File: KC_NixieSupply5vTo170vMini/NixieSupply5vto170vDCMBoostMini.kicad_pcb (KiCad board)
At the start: 2 copper layers, 38.6 x 29 mm, 42 parts, among them J1 Screw_Terminal_01x04, J2 CONN_01X01, J3 CONN_01X01, J4 CONN_01X01, J5 CONN_01X01, P1 USB_OTG, Q1 FDS2672CT, Q26 MMBTA42, U1 UCC3803

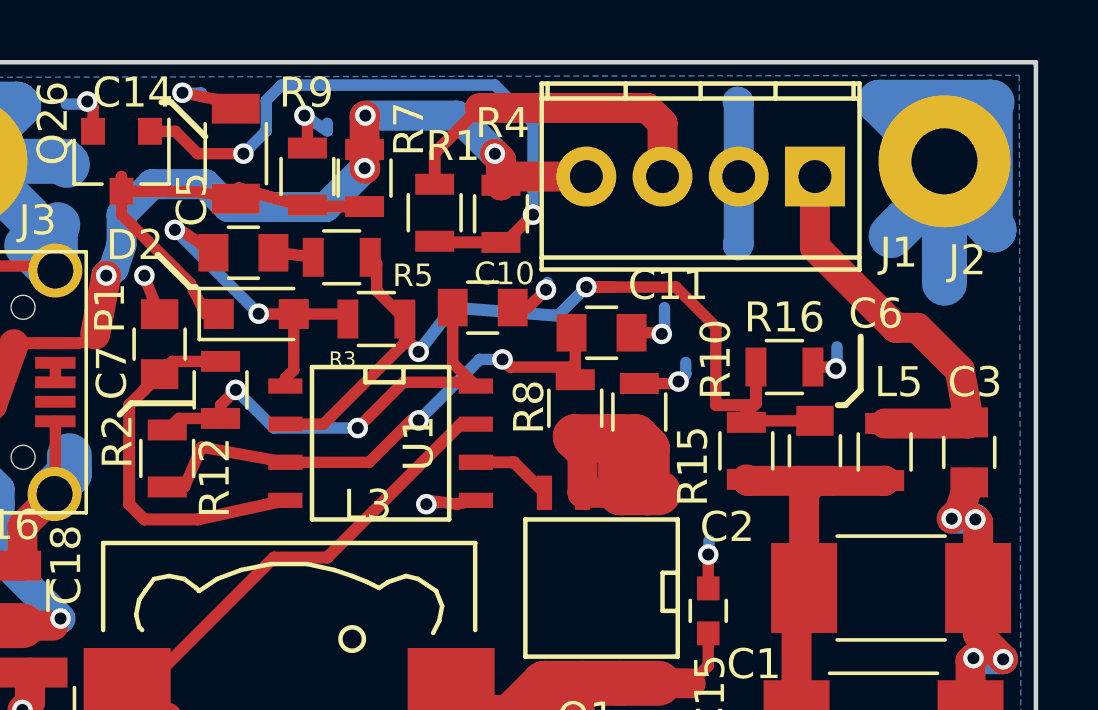
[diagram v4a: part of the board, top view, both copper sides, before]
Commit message: Updated the gerber files to include a ground pad for R10 to reduce resistance.  Also updated the net classes for the blog entry.
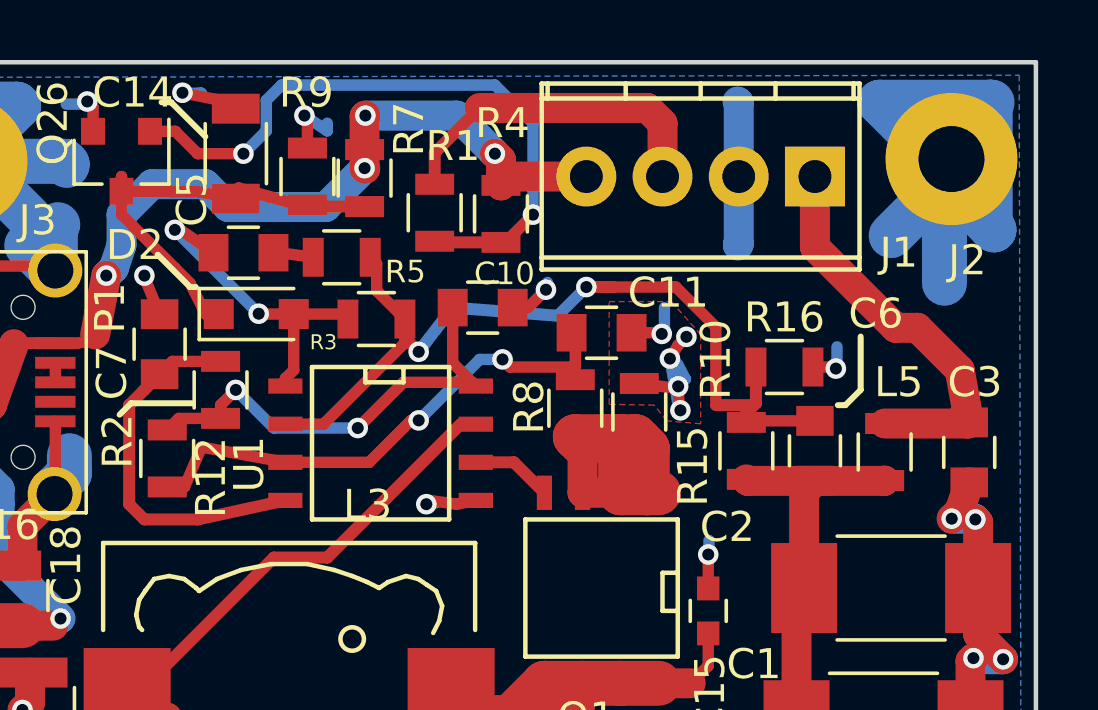
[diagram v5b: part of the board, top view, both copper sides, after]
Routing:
- net GND: track 111.5 -> 115.2 mm, vias 16 -> 19
- added copper zone on F.Cu, net GND
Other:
- net class Default: clearance 0.14 -> 0.1524
- net class Low Power Low Voltage: clearance 0.1 -> 0.1524
- net class Power Low Voltage 2A 50v: clearance 0.13 -> 0.1524
- rule trace_clearance: 0.14 -> 0.1524
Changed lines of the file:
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@@
-(kicad_pcb (version 4) (host pcbnew 4.0.7-e2-6376~60~ubuntu17.10.1)
+(kicad_pcb (version 4) (host pcbnew 4.0.7-e2-6376~58~ubuntu14.04.1)
   (general
     (links 77)
     (no_connects 0)
-    (area 17.195499 79.73792 229.894856 177.128)
+    (area 17.183099 79.73792 229.894856 177.128)
     (thickness 1.6)
     (drawings 19)
-    (tracks 347)
+    (tracks 356)
     (zones 0)
     (modules 42)
@@
     (39 F.Mask user hide)
     (41 Cmts.User user hide)
-    (44 Edge.Cuts user hide)
+    (44 Edge.Cuts user)
     (45 Margin user hide)
-    (46 B.CrtYd user hide)
-    (47 F.CrtYd user hide)
-    (48 B.Fab user hide)
-    (49 F.Fab user hide)
+    (46 B.CrtYd user)
+    (47 F.CrtYd user)
+    (48 B.Fab user)
+    (49 F.Fab user)
   )
   (setup
-    (last_trace_width 1.5)
+    (last_trace_width 0.381)
     (user_trace_width 0.2)
     (user_trace_width 0.4)
@@
     (user_trace_width 1.5)
     (user_trace_width 2)
-    (trace_clearance 0.14)
-    (zone_clearance 0.2)
+    (trace_clearance 0.1524)
+    (zone_clearance 0.1524)
     (zone_45_only no)
     (trace_min 0.1524)
@@
     (mod_text_size 1 1)
     (mod_text_width 0.15)
-    (pad_size 2.9 5.4)
-    (pad_drill 0)
+    (pad_size 4.4 4.4)
+    (pad_drill 2.2)
     (pad_to_mask_clearance 0.0508)
     (aux_axis_origin 136.0932 73.1774)
@@
   (net 21 "Net-(Q26-Pad1)")
   (net_class Default "This is the default net class."
-    (clearance 0.14)
+    (clearance 0.1524)
     (trace_width 0.381)
     (via_dia 0.6858)
@@
     (add_net "Net-(C11-Pad1)")
     (add_net "Net-(C14-Pad1)")
-    (add_net "Net-(C15-Pad1)")
     (add_net "Net-(C5-Pad1)")
     (add_net "Net-(C5-Pad2)")
@@
   )
   (net_class "Low Power Low Voltage" ""
-    (clearance 0.1)
+    (clearance 0.1524)
     (trace_width 0.381)
     (via_dia 0.6858)
@@
     (add_net +160V)
     (add_net "Net-(C1-Pad1)")
+    (add_net "Net-(C15-Pad1)")
   )
   (net_class "Power Low Voltage 2A 50v" ""
-    (clearance 0.13)
+    (clearance 0.1524)
     (trace_width 1)
     (via_dia 0.6858)
@@
     (tags "CMS SOJ")
     (attr smd)
-    (fp_text reference U1 (at 0 -1.27 270) (layer F.SilkS)
+    (fp_text reference U1 (at 0.6985 4.3815 270) (layer F.SilkS)
       (effects (font (size 1 1) (thickness 0.15)))
     )
@@
       (effects (font (size 1 1) (thickness 0.15)))
     )
-    (fp_text user %R (at 0 -1.3 270) (layer F.Fab)
+    (fp_text user %R (at -2.921 -3.2385 540) (layer F.Fab)
       (effects (font (size 1 1) (thickness 0.15)))
     )
@@
     (tags "resistor 0805")
     (attr smd)
-    (fp_text reference R5 (at -2.3749 -0.6096 180) (layer F.SilkS)
+    (fp_text reference R5 (at -2.1209 -0.4826 180) (layer F.SilkS)
       (effects (font (size 0.75 0.75) (thickness 0.15)))
     )
@@
     (tags "resistor 0805")
     (attr smd)
-    (fp_text reference R3 (at 1.1303 -1.3462 180) (layer F.SilkS)
+    (fp_text reference R3 (at 1.7653 -0.7747 180) (layer F.SilkS)
       (effects (font (size 0.5 0.5) (thickness 0.125)))
     )
@@
     (tags "capacitor 0805")
     (attr smd)
-    (fp_text reference C11 (at 2.2225 -1.5875) (layer F.SilkS)
+    (fp_text reference C11 (at 2.2225 -1.3335) (layer F.SilkS)
       (effects (font (size 1 1) (thickness 0.15)))
     )
@@
       (effects (font (size 1 1) (thickness 0.15)))
     )
-    (fp_text user %R (at 2.286 -1.651) (layer F.Fab)
+    (fp_text user %R (at 2.286 -1.397) (layer F.Fab)
       (effects (font (size 1 1) (thickness 0.15)))
     )
@@
     (fp_circle (center 0 0) (end 2.2 0) (layer Cmts.User) (width 0.15))
     (fp_circle (center 0 0) (end 2.45 0) (layer F.CrtYd) (width 0.05))
-    (pad 1 thru_hole circle (at 0 0) (size 4.4 4.4) (drill 2.2) (layers *.Cu *.Mask)
+    (pad 1 thru_hole circle (at 0.234 -0.075) (size 4.4 4.4) (drill 2.2) (layers *.Cu *.Mask)
       (net 1 GND))
   )
@@
     (tags "resistor 0805")
     (attr smd)
-    (fp_text reference R12 (at -0.635 1.5875 90) (layer F.SilkS)
+    (fp_text reference R12 (at -0.635 1.4605 90) (layer F.SilkS)
       (effects (font (size 1 1) (thickness 0.15)))
     )
@@
     (fp_line (start -6.4 -6.5) (end 6.4 -6.5) (layer F.Fab) (width 0.15))
     (fp_line (start 6.4 -6.5) (end 6.3 -3.2) (layer F.Fab) (width 0.15))
-    (fp_text user %R (at -2.7432 7.4676 180) (layer F.Fab)
+    (fp_text user %R (at 1.8415 7.112 180) (layer F.Fab)
       (effects (font (size 1 1) (thickness 0.15)))
     )
@@
   )
   (segment (start 17.526 143.2633) (end 17.526 142.9893) (width 0.381) (layer F.Cu) (net 0))
+  (segment (start 162.298 91.92) (end 162.573 91.47) (width 0.381) (layer F.Cu) (net 1))
+  (segment (start 162.6104 93.6074) (end 162.648 93.645) (width 0.381) (layer F.Cu) (net 1))
+  (via (at 162.648 93.645) (size 0.6858) (drill 0.4) (layers F.Cu B.Cu) (net 1))
+  (segment (start 162.648 93.645) (end 162.598 93.595) (width 0.381) (layer B.Cu) (net 1))
+  (segment (start 162.598 93.595) (end 162.298 91.92) (width 0.381) (layer B.Cu) (net 1))
+  (via (at 162.298 91.92) (size 0.6858) (drill 0.4) (layers F.Cu B.Cu) (net 1))
+  (segment (start 162.573 92.845) (end 162.6104 93.6074) (width 0.381) (layer F.Cu) (net 1))
+  (via (at 162.848 91.195) (size 0.6858) (drill 0.4) (layers F.Cu B.Cu) (net 1))
+  (segment (start 162.573 91.47) (end 162.848 91.195) (width 0.381) (layer F.Cu) (net 1))
   (segment (start 137.287 83.439) (end 137.287 87.249) (width 1.5) (layer B.Cu) (net 1))
   (segment (start 137.287 87.249) (end 137.0965 87.4395) (width 1.5) (layer B.Cu) (net 1))
@@
   (segment (start 164.5666 88.1253) (end 164.5666 88.1507) (width 1) (layer B.Cu) (net 1))
   (segment (start 164.592 88.0999) (end 164.5666 88.1253) (width 1) (layer B.Cu) (net 1))
-  (segment (start 161.2773 92.7506) (end 162.5194 92.7506) (width 0.381) (layer F.Cu) (net 1))
-  (segment (start 162.8267 92.4433) (end 162.8267 92.0496) (width 0.381) (layer B.Cu) (net 1))
-  (segment (start 162.5854 92.6846) (end 162.8267 92.4433) (width 0.381) (layer B.Cu) (net 1))
-  (via (at 162.5854 92.6846) (size 0.6858) (drill 0.4) (layers F.Cu B.Cu) (net 1))
-  (segment (start 162.5194 92.7506) (end 162.5854 92.6846) (width 0.381) (layer F.Cu) (net 1))
+  (segment (start 161.2773 92.7506) (end 162.507 92.911) (width 0.381) (layer F.Cu) (net 1))
+  (segment (start 162.8143 92.6037) (end 162.5517 92.0996) (width 0.381) (layer B.Cu) (net 1))
+  (segment (start 162.573 92.845) (end 162.8143 92.6037) (width 0.381) (layer B.Cu) (net 1))
+  (via (at 162.573 92.845) (size 0.6858) (drill 0.4) (layers F.Cu B.Cu) (net 1))
+  (segment (start 162.507 92.911) (end 162.573 92.845) (width 0.381) (layer F.Cu) (net 1))
   (segment (start 161.02 91.059) (end 161.9885 91.059) (width 0.381) (layer F.Cu) (net 1))
   (segment (start 162.1155 91.0082) (end 162.1155 90.2208) (width 0.381) (layer B.Cu) (net 1))
@@
       )
     )
+  )
+  (zone (net 1) (net_name GND) (layer F.Cu) (hatch edge 0.508)
+    (connect_pads yes (clearance 0.1524))
+    (min_thickness 0.254)
+    (fill yes (arc_segments 16) (thermal_gap 0.7) (thermal_bridge_width 0.7))
+    (polygon
+      (pts
+        (xy 163.323 91.12) (xy 163.323 94.095) (xy 162.198 93.995) (xy 161.773 93.47) (xy 160.273 93.445)
+        (xy 160.273 90.02) (xy 162.348 90.02)
+      )
+    )

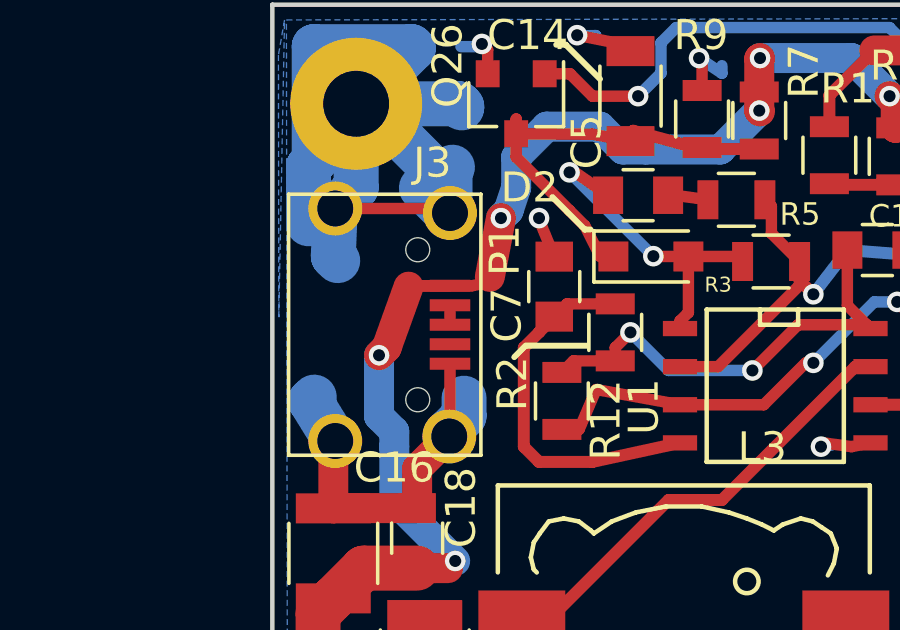
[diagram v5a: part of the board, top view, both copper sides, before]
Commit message: New Rev 3 for the Original Nixie Power Supply 1. Corner Mounting Holes are now Solid.  Per the tip by comment reader 2. The original supply has a better ground connection for the USB input,     But the USB connector shield is still grounded. 2.5. The D+ and D- USB inputs are unshorted. 3. The revision was updated to Rev 3 for the Original Supply and Rev 2 for the Mini Supply 4. New Gerbers were created and zip files
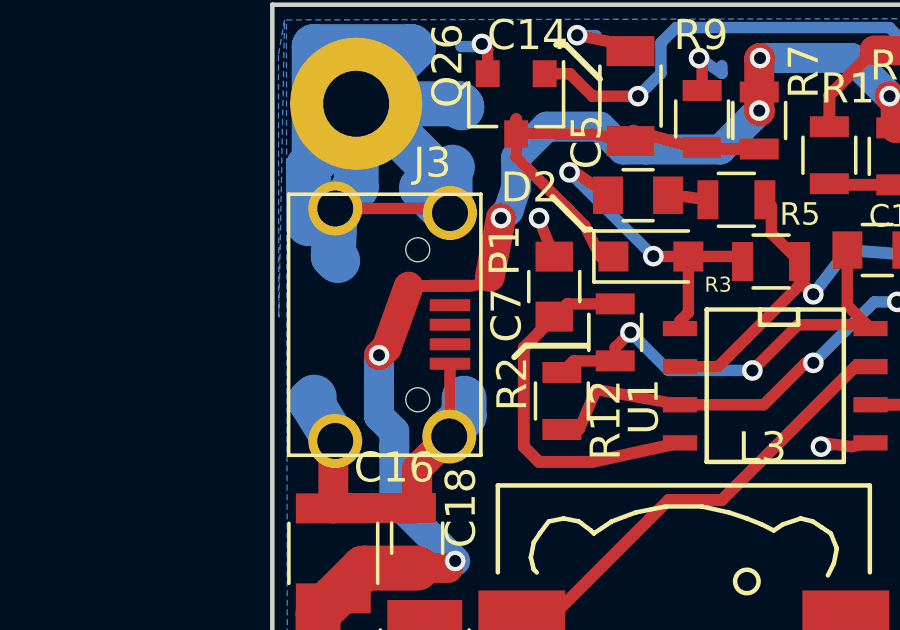
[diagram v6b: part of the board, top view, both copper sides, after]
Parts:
- C7: value 330pF -> 430pF
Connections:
- P1 pad 3: Net-(P1-Pad2) -> Net-(P1-Pad3)
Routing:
- net Net-(P1-Pad2): track 0.65 -> 0.00 mm
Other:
- board text added: "NixieSupplyMini Rev2_1810"
- board text removed: "NixieSupplyMini Rev1_1804"
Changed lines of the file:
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@@
-(kicad_pcb (version 4) (host pcbnew 4.0.7-e2-6376~58~ubuntu14.04.1)
+(kicad_pcb (version 4) (host pcbnew 4.0.6+dfsg1-1)
   (general
-    (links 77)
+    (links 76)
     (no_connects 0)
     (area 17.183099 79.73792 229.894856 177.128)
     (thickness 1.6)
     (drawings 19)
-    (tracks 356)
+    (tracks 355)
     (zones 0)
     (modules 42)
-    (nets 22)
+    (nets 23)
   )
   (page A4)
@@
   (net 20 "Net-(C9-Pad1)")
   (net 21 "Net-(Q26-Pad1)")
+  (net 22 "Net-(P1-Pad3)")
   (net_class Default "This is the default net class."
     (clearance 0.1524)
@@
     (add_net "Net-(J4-Pad1)")
     (add_net "Net-(J5-Pad1)")
+    (add_net "Net-(P1-Pad3)")
     (add_net "Net-(Q1-Pad1)")
     (add_net "Net-(Q26-Pad1)")
@@
       (net 11 "Net-(P1-Pad2)"))
     (pad 3 smd rect (at 0 -1.35) (size 1.35 0.4) (layers F.Cu F.Paste F.Mask)
-      (net 11 "Net-(P1-Pad2)"))
+      (net 22 "Net-(P1-Pad3)"))
     (pad 4 smd rect (at 0.65 -1.35) (size 1.35 0.4) (layers F.Cu F.Paste F.Mask)
       (net 12 "Net-(P1-Pad4)"))
@@
       (effects (font (size 1 1) (thickness 0.15)))
     )
-    (fp_text value 330pF (at 0 1.75 90) (layer F.Fab)
+    (fp_text value 430pF (at 0 1.75 90) (layer F.Fab)
       (effects (font (size 1 1) (thickness 0.15)))
     )
@@
     (fp_circle (center 0 0) (end 2.45 0) (layer F.CrtYd) (width 0.05))
     (pad 1 thru_hole circle (at 0.234 -0.075) (size 4.4 4.4) (drill 2.2) (layers *.Cu *.Mask)
-      (net 1 GND))
+      (net 1 GND) (zone_connect 2))
   )
   (module Mounting_Holes:MountingHole_2.2mm_M2_Pad (layer F.Cu)
@@
     (fp_circle (center 0 0) (end 2.45 0) (layer F.CrtYd) (width 0.05))
     (pad 1 thru_hole circle (at 0 0) (size 4.4 4.4) (drill 2.2) (layers *.Cu *.Mask)
-      (net 1 GND))
+      (net 1 GND) (zone_connect 2))
   )
   (module Capacitors_SMD:C_0805 (layer F.Cu)
@@
     (effects (font (size 1 1.5) (thickness 0.2)) (justify mirror))
   )
-  (gr_text "NixieSupplyMini Rev1_1804" (at 155.448 98.8695) (layer B.SilkS)
+  (gr_text "NixieSupplyMini Rev2_1810" (at 155.448 98.8695) (layer B.SilkS)
     (effects (font (size 1.5 1.5) (thickness 0.3)) (justify mirror))
   )
@@
   (segment (start 137.414 103.444) (end 137.414 102.338) (width 1.5) (layer F.Cu) (net 10))
   (segment (start 137.414 102.338) (end 137.922 101.83) (width 1.5) (layer F.Cu) (net 10))
-  (segment (start 141.812 92.06) (end 141.812 92.71) (width 0.381) (layer F.Cu) (net 11))
   (segment (start 167.132 95.996) (end 164.896 95.996) (width 1) (layer F.Cu) (net 13))
   (segment (start 164.896 95.996) (end 164.846 95.946) (width 1) (layer F.Cu) (net 13))

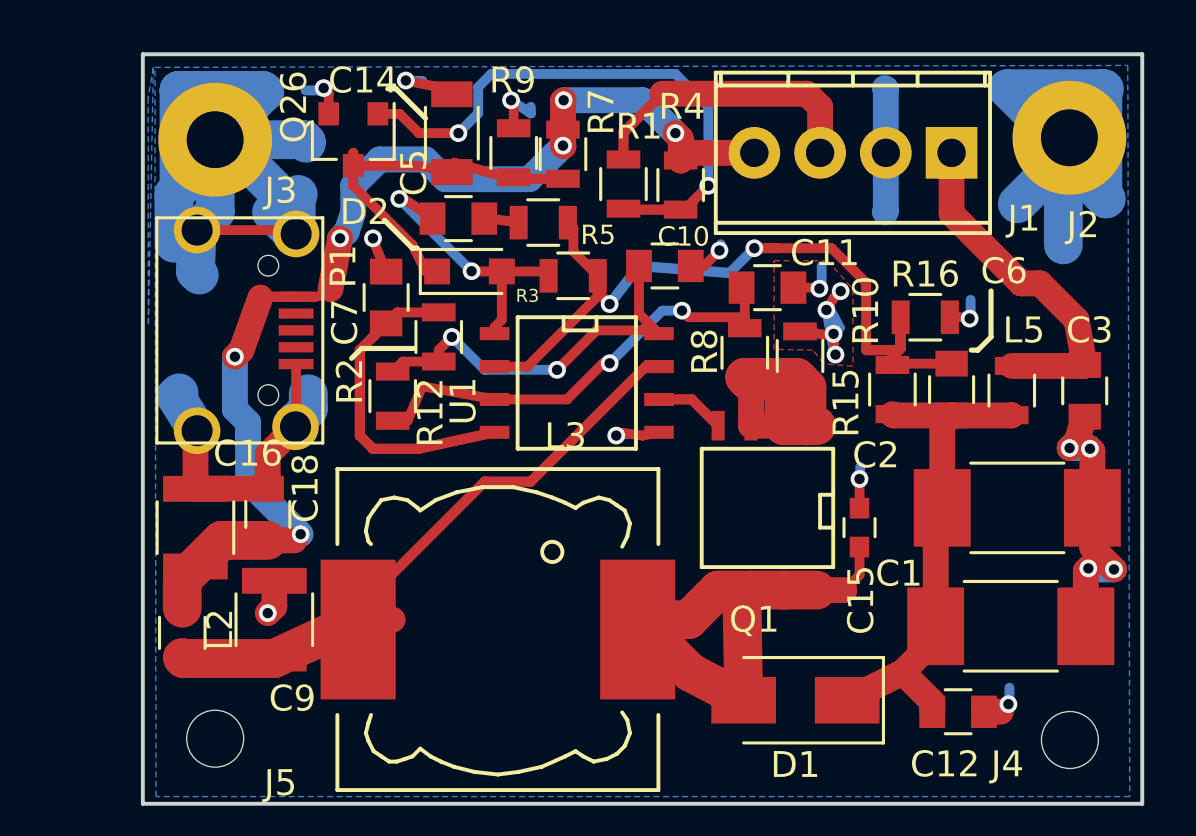
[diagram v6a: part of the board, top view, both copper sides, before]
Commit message: Rev 3 of the Mini Nixie Tube Power supply schematic and layout. Changed the output connector to have 1.25mm spacing with nearest conductor
Moved traces around to allow forn two output connectors.    Changed
the size of the 47uF 16v capacitor to a 1210 package.
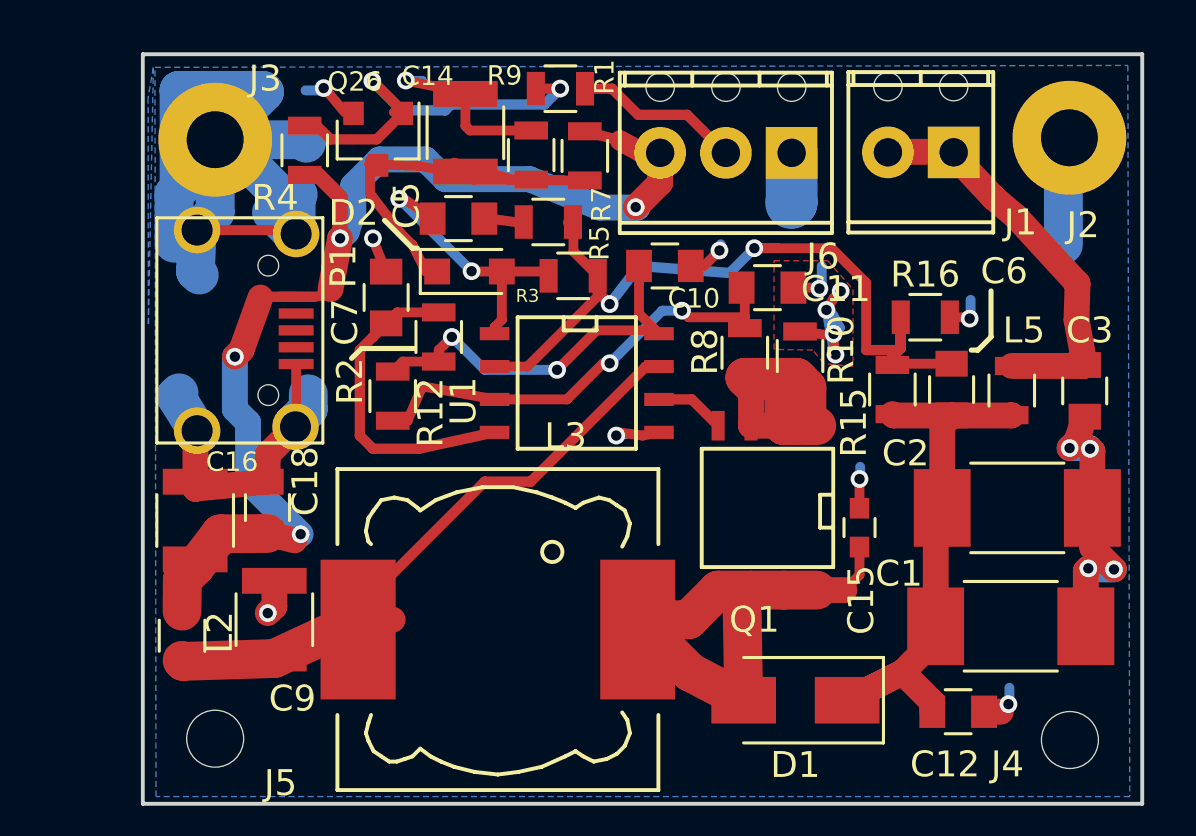
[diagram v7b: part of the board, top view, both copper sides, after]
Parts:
- added J6: Screw_Terminal_1x03, TerminalBlock_Phoenix:TerminalBlock_Phoenix_MPT-2.54mm_3pol, F.Cu at (161.0, 85.9)
- C14: footprint Capacitors_SMD:C_1206 -> Capacitors_SMD:C_1210
- J1: value Screw_Terminal_01x04 -> Screw_Terminal_1x02; footprint TerminalBlock_Phoenix:TerminalBlock_Phoenix_MPT-2.54mm_4pol -> TerminalBlock_Phoenix:TerminalBlock_Phoenix_MPT-2.54mm_2pol
- moved R4 14.6 mm to (142.1, 85.8), turned to 270 degrees
- moved R1 4.42 mm to (152.0, 83.4), turned to 0 degrees
- moved Q26 0.96 mm to (145.0, 85.3)
- moved R7 0.85 mm to (153.0, 86.0)
- moved R9 0.68 mm to (150.9, 85.9)
- moved C14 0.52 mm to (148.4, 85.1)
- moved C16 0.27 mm to (137.9, 100.1)
- moved C18 0.27 mm to (140.7, 99.6)
- moved R5 0.20 mm to (151.6, 88.5)
- moved L2 0.11 mm to (137.4, 104.5)
- moved J1 0.08 mm to (167.2, 85.8)
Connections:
- J1 pad 2: GND -> +160V
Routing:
- net GND: track 115.2 -> 94.8 mm, vias 19 -> 18
- net Net-(Q26-Pad1): track 21.9 -> 15.4 mm
- net N_ENABLE: track 11.2 -> 6.47 mm
- net Net-(C14-Pad1): track 15.1 -> 18.2 mm
- net +160V: track 13.5 -> 15.6 mm
- net 5v_Power: track 45.3 -> 46.4 mm, vias 6 -> 4
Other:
- board text added: "NixieSupplyMini Rev3_1812"
- board text removed: "NixieSupplyMini Rev2_1810"
